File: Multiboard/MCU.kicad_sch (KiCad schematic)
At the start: 46 parts, among them J1 Conn_01x20_Socket, J2 Conn_01x20_Socket, J3 Debug, J4 USB_C_Receptacle_USB2.0_16P, SW1 BOOT0, SW2 NRST, SW7 KEY, U1 STM32F411RET6, U2 MAX662AESA_T, U3 ME6211C33M5, U9 USBLC6-2SC6, Y1 32.768KHz, Y2 25MHz

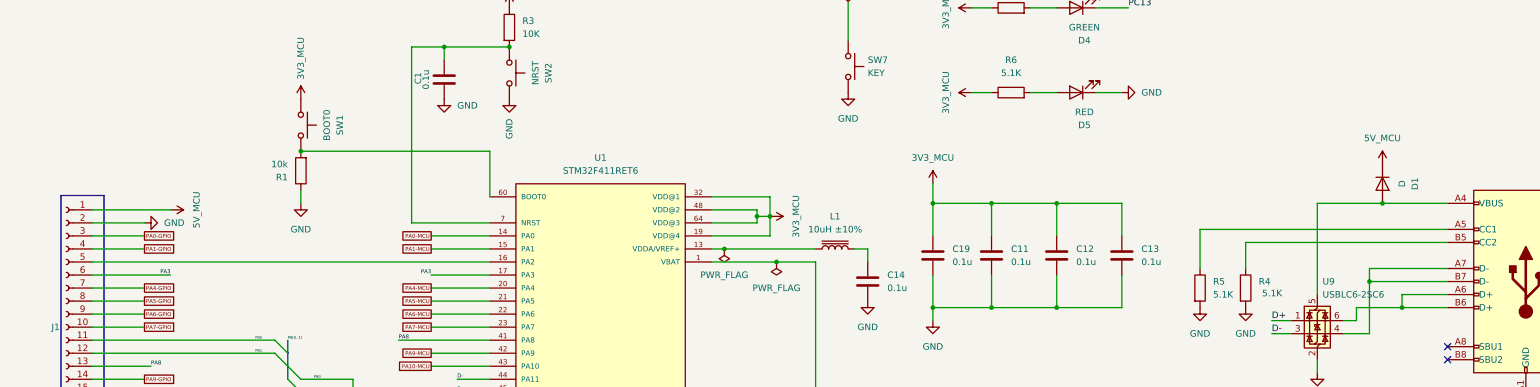
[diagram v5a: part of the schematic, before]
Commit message: Restored older version due to KiCAD glitching
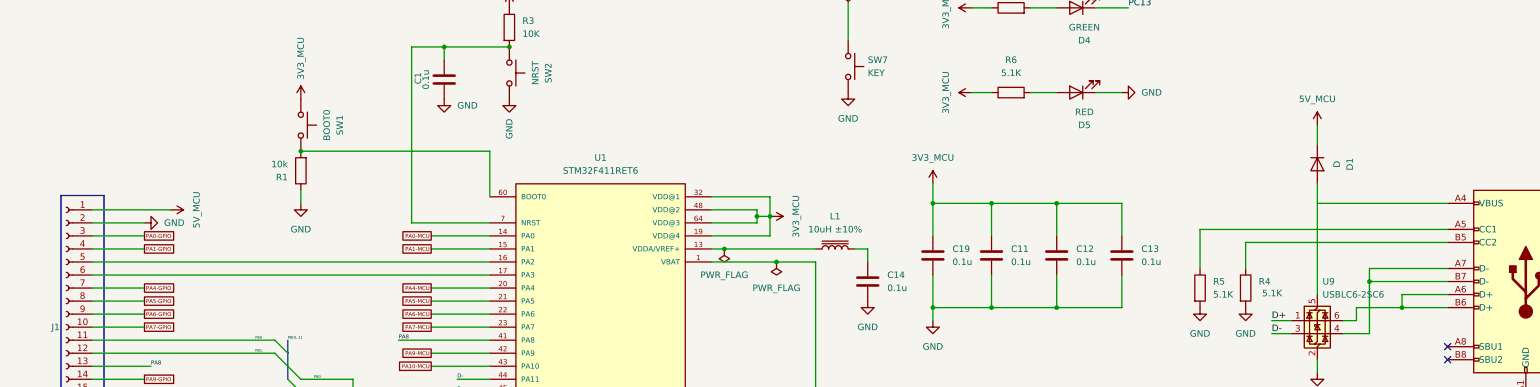
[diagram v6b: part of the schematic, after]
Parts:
- U3: footprint Package_TO_SOT_SMD:SOT-23-5 -> Package_TO_SOT_SMD:SOT-23-5_HandSoldering; LCSC Part Number C2984946 -> (none)
- Y1: LCSC Part Number C95361 -> (none)
- Y2: LCSC Part Number C255920 -> (none)
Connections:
- net at J4.A4 (VBUS), J4.A9 (VBUS), J4.B4 (VBUS)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: no longer D1.2 (A), U9.5 (VBUS)
- net PA3: no longer names the net of J1.6 (Pin_6), U1.17 (PA3)
- new net: D1.2 (A), U9.5 (VBUS)
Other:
- moved on the sheet: D1
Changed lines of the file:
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@@
 	)
 	(junction
-		(at 330.2 60.96)
-		(diameter 0)
-		(color 0 0 0 0)
-	)
-	(junction
 		(at 364.49 123.19)
 		(diameter 0)
@@
 	(wire
 		(pts
-			(xy 144.78 74.93) (xy 156.21 74.93)
+			(xy 78.74 100.33) (xy 88.9 100.33)
 		)
 		(stroke
@@
 	(wire
 		(pts
-			(xy 78.74 100.33) (xy 88.9 100.33)
+			(xy 201.93 69.85) (xy 219.71 69.85)
 		)
 		(stroke
@@
 	(wire
 		(pts
-			(xy 201.93 69.85) (xy 219.71 69.85)
+			(xy 341.63 123.19) (xy 335.28 123.19)
 		)
 		(stroke
@@
 	(wire
 		(pts
-			(xy 341.63 123.19) (xy 335.28 123.19)
+			(xy 219.71 123.19) (xy 219.71 138.43)
 		)
 		(stroke
@@
 	(wire
 		(pts
-			(xy 219.71 123.19) (xy 219.71 138.43)
+			(xy 364.49 123.19) (xy 364.49 124.46)
 		)
 		(stroke
@@
 	(wire
 		(pts
-			(xy 364.49 123.19) (xy 364.49 124.46)
+			(xy 317.5 45.72) (xy 317.5 49.53)
 		)
 		(stroke
@@
 	(wire
 		(pts
+			(xy 317.5 57.15) (xy 317.5 78.74)
+		)
+		(stroke
+			(width 0)
+			(type default)
+		)
+	)
+	(wire
+		(pts
 			(xy 119.38 58.42) (xy 119.38 60.96)
 		)
@@
 	(wire
 		(pts
-			(xy 317.5 60.96) (xy 330.2 60.96)
+			(xy 317.5 60.96) (xy 342.9 60.96)
 		)
 		(stroke
@@
 	(wire
 		(pts
-			(xy 317.5 78.74) (xy 317.5 60.96)
-		)
-		(stroke
-			(width 0)
-			(type default)
-		)
-	)
-	(wire
-		(pts
 			(xy 119.38 179.07) (xy 127 179.07)
 		)
@@
 	(wire
 		(pts
-			(xy 78.74 74.93) (xy 93.98 74.93)
+			(xy 335.28 116.84) (xy 335.28 123.19)
 		)
 		(stroke
@@
 	(wire
 		(pts
-			(xy 335.28 116.84) (xy 335.28 123.19)
+			(xy 78.74 74.93) (xy 156.21 74.93)
 		)
 		(stroke
@@
 	(wire
 		(pts
-			(xy 330.2 60.96) (xy 342.9 60.96)
-		)
-		(stroke
-			(width 0)
-			(type default)
-		)
-	)
-	(wire
-		(pts
 			(xy 308.61 86.36) (xy 312.42 86.36)
 		)
@@
 		)
 	)
-	(label "PA3"
-		(at 93.98 74.93 180)
-		(effects
-			(font
-				(size 0.762 0.762)
-			)
-			(justify right bottom)
-		)
-	)
 	(label "PB12"
 		(at 120.65 146.05 0)
@@
 		)
 	)
-	(label "PA3"
-		(at 144.78 74.93 180)
-		(effects
-			(font
-				(size 0.762 0.762)
-			)
-			(justify right bottom)
-		)
-	)
 	(label "D+"
 		(at 308.61 83.82 0)
@@
 	(symbol
 		(lib_id "Device:D")
-		(at 330.2 57.15 270)
+		(at 317.5 53.34 270)
 		(unit 1)
 		(exclude_from_sim no)
@@
 		(fields_autoplaced yes)
 		(property "Reference" "D1"
-			(at 336.55 57.15 0)
+			(at 323.85 53.34 0)
 			(effects
 				(font
@@
 		)
 		(property "Value" "D"
-			(at 334.01 57.15 0)
+			(at 321.31 53.34 0)
 			(effects
 				(font
@@
 		)
 		(property "Footprint" "Diode_SMD:D_0603_1608Metric_Pad1.05x0.95mm_HandSolder"
-			(at 330.2 57.15 0)
+			(at 317.5 53.34 0)
 			(effects
 				(font
@@
 		)
 		(property "Datasheet" "~"
-			(at 330.2 57.15 0)
+			(at 317.5 53.34 0)
 			(effects
 				(font
@@
 		)
 		(property "Description" "Diode"
-			(at 330.2 57.15 0)
+			(at 317.5 53.34 0)
 			(effects
 				(font
@@
 		)
 		(property "Sim.Device" "D"
-			(at 330.2 57.15 0)
+			(at 317.5 53.34 0)
 			(effects
 				(font
@@
 		)
 		(property "Sim.Pins" "1=K 2=A"
-			(at 330.2 57.15 0)
+			(at 317.5 53.34 0)
 			(effects
 				(font
@@
 		)
 		(property "LCSC Part Number" ""
-			(at 330.2 57.15 0)
+			(at 317.5 53.34 0)
 			(effects
 				(font
@@
 	(symbol
 		(lib_id "power:VCC")
-		(at 330.2 53.34 0)
+		(at 317.5 45.72 0)
 		(unit 1)
 		(exclude_from_sim no)
@@
 		(fields_autoplaced yes)
 		(property "Reference" "#PWR0137"
-			(at 330.2 57.15 0)
+			(at 317.5 49.53 0)
 			(effects
 				(font
@@
 		)
 		(property "Value" "5V_MCU"
-			(at 330.2 48.26 0)
+			(at 317.5 40.64 0)
 			(do_not_autoplace yes)
 			(effects
@@
 		)
 		(property "Footprint" ""
-			(at 330.2 53.34 0)
+			(at 317.5 45.72 0)
 			(effects
 				(font
@@
 		)
 		(property "Datasheet" ""
-			(at 330.2 53.34 0)
+			(at 317.5 45.72 0)
 			(effects
 				(font
@@
 		)
 		(property "Description" "Power symbol creates a global label with name \"VCC\""
-			(at 330.2 53.34 0)
+			(at 317.5 45.72 0)
 			(effects
 				(font
@@
 			)
 		)
-		(property "LCSC Part Number" "C255920"
+		(property "LCSC Part Number" ""
 			(at 127 210.82 90)
 			(effects
@@
 	)
 	(symbol
-		(lib_id "Regulator_Linear:ME6211C33M5")
-		(at 349.25 125.73 0)
-		(unit 1)
-		(exclude_from_sim no)
-		(in_bom yes)
-		(on_board yes)
-		(dnp no)
-		(fields_autoplaced yes)
-		(property "Reference" "U3"
-			(at 349.25 115.57 0)
-			(effects
-				(font
-					(size 1.27 1.27)
-				)
-			)
-		)
-		(property "Value" "ME6211C33M5"
-			(at 349.25 118.11 0)
-			(effects
-				(font
-					(size 1.27 1.27)
-				)
-			)
-		)
-		(property "Footprint" "Package_TO_SOT_SMD:SOT-23-5"
-			(at 348.742 139.192 0)
-			(effects
-				(font
-					(size 1.27 1.27)
-				)
-				(hide yes)
-			)
-		)
-		(property "Datasheet" "https://www.lcsc.com/datasheet/lcsc_datasheet_2304140030_MICRONE-Nanjing-Micro-One-Elec-ME6211C33R5G_C235316.pdf"
-			(at 349.504 142.748 0)
-			(effects
-				(font
-					(size 1.27 1.27)
-				)
-				(hide yes)
-			)
-		)
-		(property "Description" "500mA low dropout linear regulator, shutdown pin, 6.5V max input voltage, 3.3V fixed positive output, SOT-23-5"
-			(at 351.028 140.97 0)
-			(effects
-				(font
-					(size 1.27 1.27)
-				)
-				(hide yes)
-			)
-		)
-		(property "LCSC Part Number" "C2984946"
-			(at 349.25 125.73 0)
-			(effects
-				(font
-					(size 1.27 1.27)
-				)
-				(hide yes)
-			)
-		)
-		(pin "2"
-		)
-		(pin "5"
-		)
-		(pin "4"
-		)
-		(pin "3"
-		)
-		(pin "1"
-		)
-		(instances
-			(project ""
-				(path "/9ed4a389-3aa7-41f1-b239-280eb7f09ef1/2bca3eb5-73b3-4aa8-9f30-e1743a374253"
-					(reference "U3")
-					(unit 1)
-				)
-			)
-		)
-	)
-	(symbol
 		(lib_id "power:GND")
 		(at 88.9 64.77 90)
@@
 			)
 		)
-		(property "LCSC Part Number" "C95361"
+		(property "LCSC Part Number" ""
 			(at 127 185.42 90)
 			(effects
@@
 					(unit 1)
 				)
+			)
+		)
+	)
+	(symbol
+		(lib_id "Regulator_Linear:ME6211C33M5")
+		(at 349.25 125.73 0)
+		(unit 1)
+		(exclude_from_sim no)
+		(in_bom yes)
+		(on_board yes)
+		(dnp no)
+		(fields_autoplaced yes)
+		(property "Reference" "U3"
+			(at 349.25 115.57 0)
+			(effects
+				(font
+					(size 1.27 1.27)
+				)
+			)
+		)
+		(property "Value" "ME6211C33M5"
+			(at 349.25 118.11 0)
+			(effects
+				(font
+					(size 1.27 1.27)
+				)
+			)
+		)
+		(property "Footprint" "Package_TO_SOT_SMD:SOT-23-5_HandSoldering"
+			(at 348.742 139.192 0)
+			(effects
+				(font
+					(size 1.27 1.27)
+				)
+				(hide yes)
+			)
+		)
+		(property "Datasheet" "https://www.lcsc.com/datasheet/lcsc_datasheet_2304140030_MICRONE-Nanjing-Micro-One-Elec-ME6211C33R5G_C235316.pdf"
+			(at 349.504 142.748 0)
+			(effects
+				(font
+					(size 1.27 1.27)
+				)
+				(hide yes)
+			)
+		)
+		(property "Description" "500mA low dropout linear regulator, shutdown pin, 6.5V max input voltage, 3.3V fixed positive output, SOT-23-5"
+			(at 351.028 140.97 0)
+			(effects
+				(font
+					(size 1.27 1.27)
+				)
+				(hide yes)
+			)
+		)
+		(pin "5"
+		)
+		(pin "2"
+		)
+		(pin "4"
+		)
+		(pin "1"
+		)
+		(pin "3"
+		)
+		(instances
+			(project ""
+				(path "/9ed4a389-3aa7-41f1-b239-280eb7f09ef1/2bca3eb5-73b3-4aa8-9f30-e1743a374253"
+					(reference "U3")
+					(unit 1)
+				)

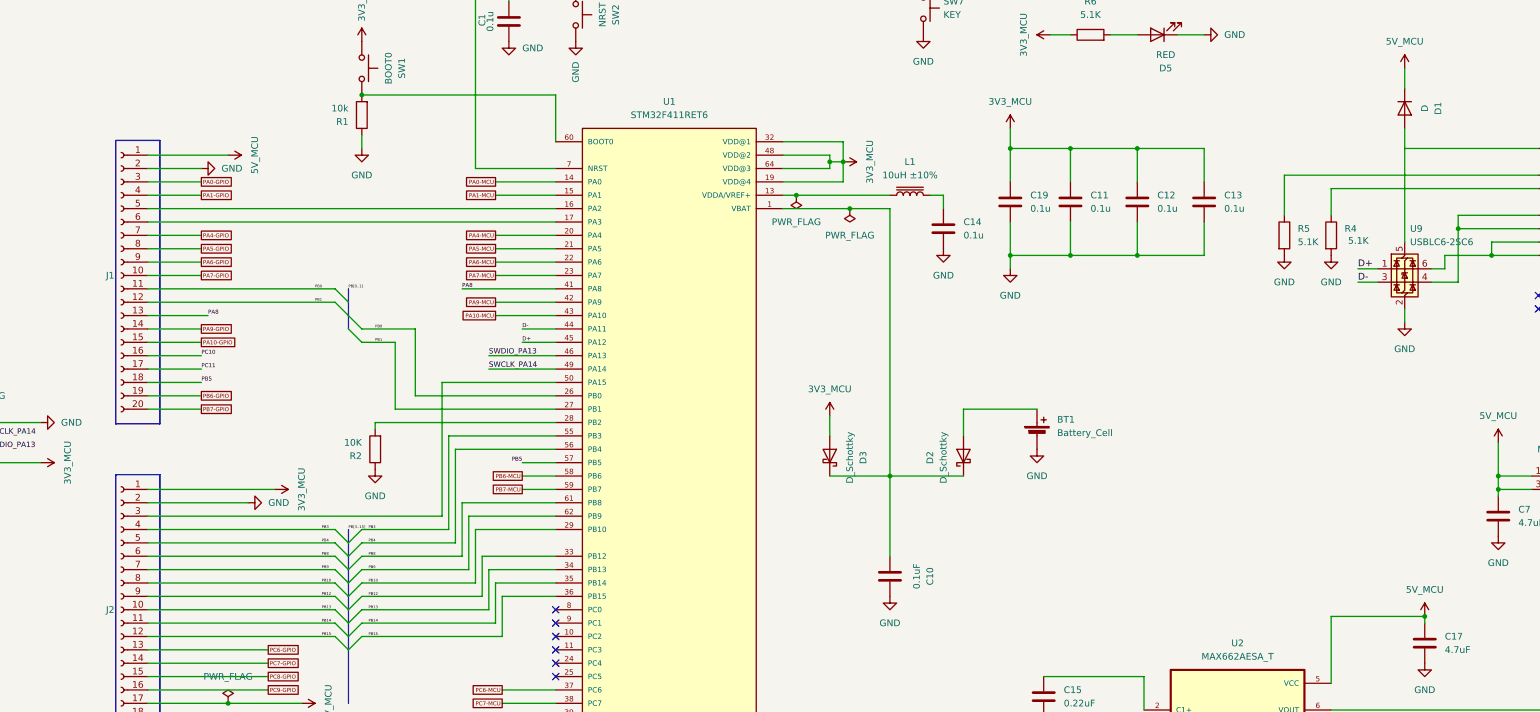
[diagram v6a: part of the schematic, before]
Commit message: Fixed glitched nets issue
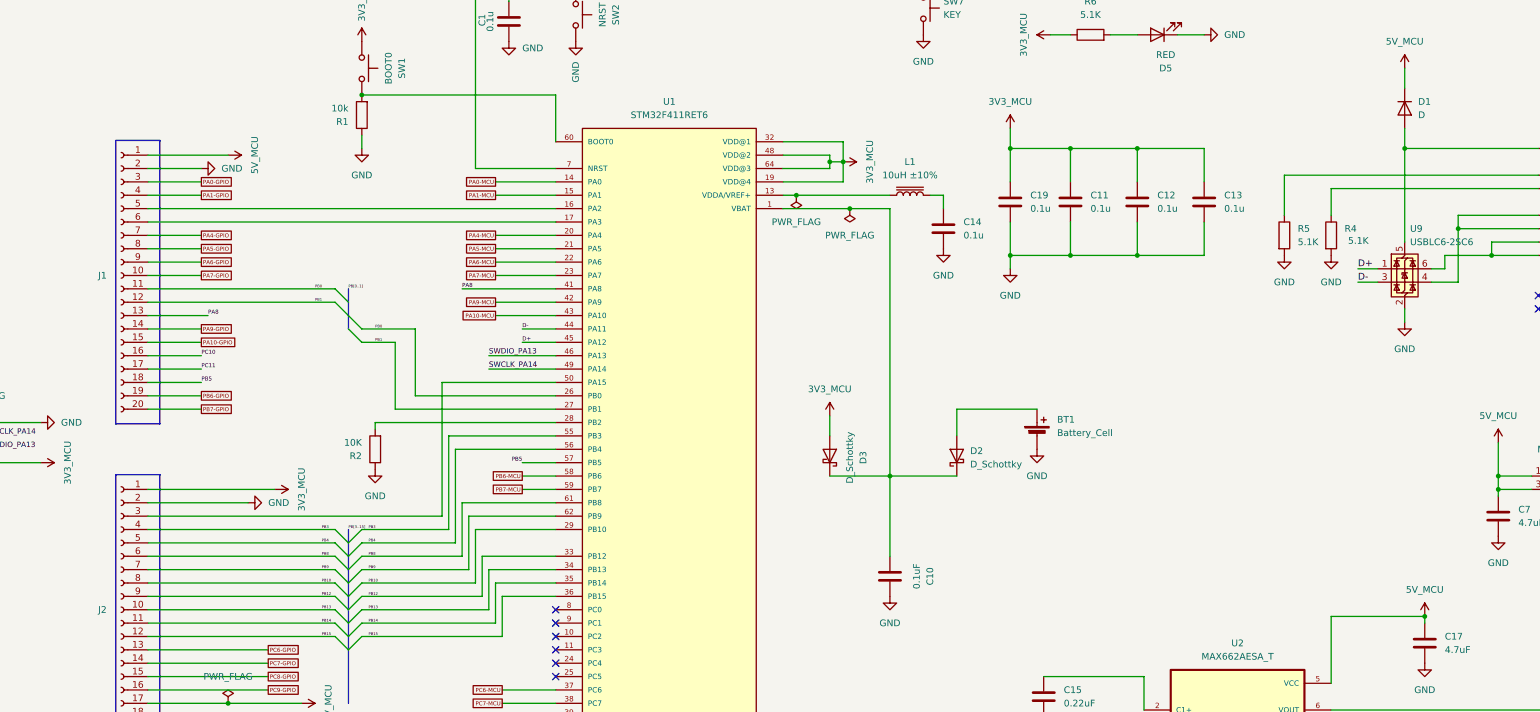
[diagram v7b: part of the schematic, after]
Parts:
- BT1, D1, J1, J2, J3: now left out of the parts list
- U3: LCSC Part Number (none) -> C2984946
- Y1: LCSC Part Number (none) -> C95361
- Y2: LCSC Part Number (none) -> C255920
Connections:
- net at D1.2 (A), U9.5 (VBUS): now also J4.A4 (VBUS), J4.A9 (VBUS), J4.B4 (VBUS), J4.B9 (VBUS)
